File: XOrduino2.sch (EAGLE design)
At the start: 82 parts, among them J1 2.5mm, J2 2.5mm, J3 2.5mm, J4 2.5mm, J5 Batt In, J6 MOT R, J7 MOT L, P1 10k, Q1 ALS-PT204-6C/L177, SW1 RESET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

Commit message: v7: Update USB mini-B footprint & bom; more heat sink area for motor driver.
Went through and widened power traces as much as I could, as well.
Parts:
- JP9: device xorduino:SOLDERJUMPERBOT-VIA-NOCONFLICT -> xorduino:SOLDERJUMPERBOT-NOCONFLICT
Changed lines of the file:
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@@
 <part name="JP8" library="xorduino" deviceset="SOLDERJUMPER" device="BOT-VIA-NOCONFLICT" value="N/C"/>
 <part name="JP7" library="xorduino" deviceset="SOLDERJUMPER" device="BOT-VIA-NOCONFLICT" value="N/C"/>
-<part name="JP9" library="xorduino" deviceset="SOLDERJUMPER" device="BOT-VIA-NOCONFLICT" value="N/C"/>
+<part name="JP9" library="xorduino" deviceset="SOLDERJUMPER" device="BOT-NOCONFLICT" value="N/C"/>
 <part name="JP1" library="xorduino" deviceset="SOLDERJUMPER" device="NOCONFLICT" value="N/C"/>
 <part name="JP10" library="xorduino" deviceset="SOLDERJUMPER" device="BOT-VIA-NOCONFLICT" value="N/C"/>
@@
 <text x="-120.142" y="-31.496" size="1.27" layer="97">optional</text>
 <text x="169.926" y="43.434" size="1.27" layer="97">optional</text>
-<text x="189.23" y="-58.928" size="2.54" layer="97">6</text>
+<text x="189.23" y="-58.928" size="2.54" layer="97">7</text>
 <text x="192.024" y="-69.088" size="2.54" layer="97">CSA</text>
 <text x="40.64" y="30.48" size="3.81" layer="94" ratio="10" rot="MR0">Scratch Sensor Board</text>

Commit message: Minor silkscreen tweaks, extend L3 pads a hair.
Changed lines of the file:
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@@
 <text x="-120.142" y="-31.496" size="1.27" layer="97">optional</text>
 <text x="169.926" y="43.434" size="1.27" layer="97">optional</text>
-<text x="189.23" y="-58.928" size="2.54" layer="97">7</text>
+<text x="189.23" y="-58.928" size="2.54" layer="97">8</text>
 <text x="192.024" y="-69.088" size="2.54" layer="97">CSA</text>
 <text x="40.64" y="30.48" size="3.81" layer="94" ratio="10" rot="MR0">Scratch Sensor Board</text>

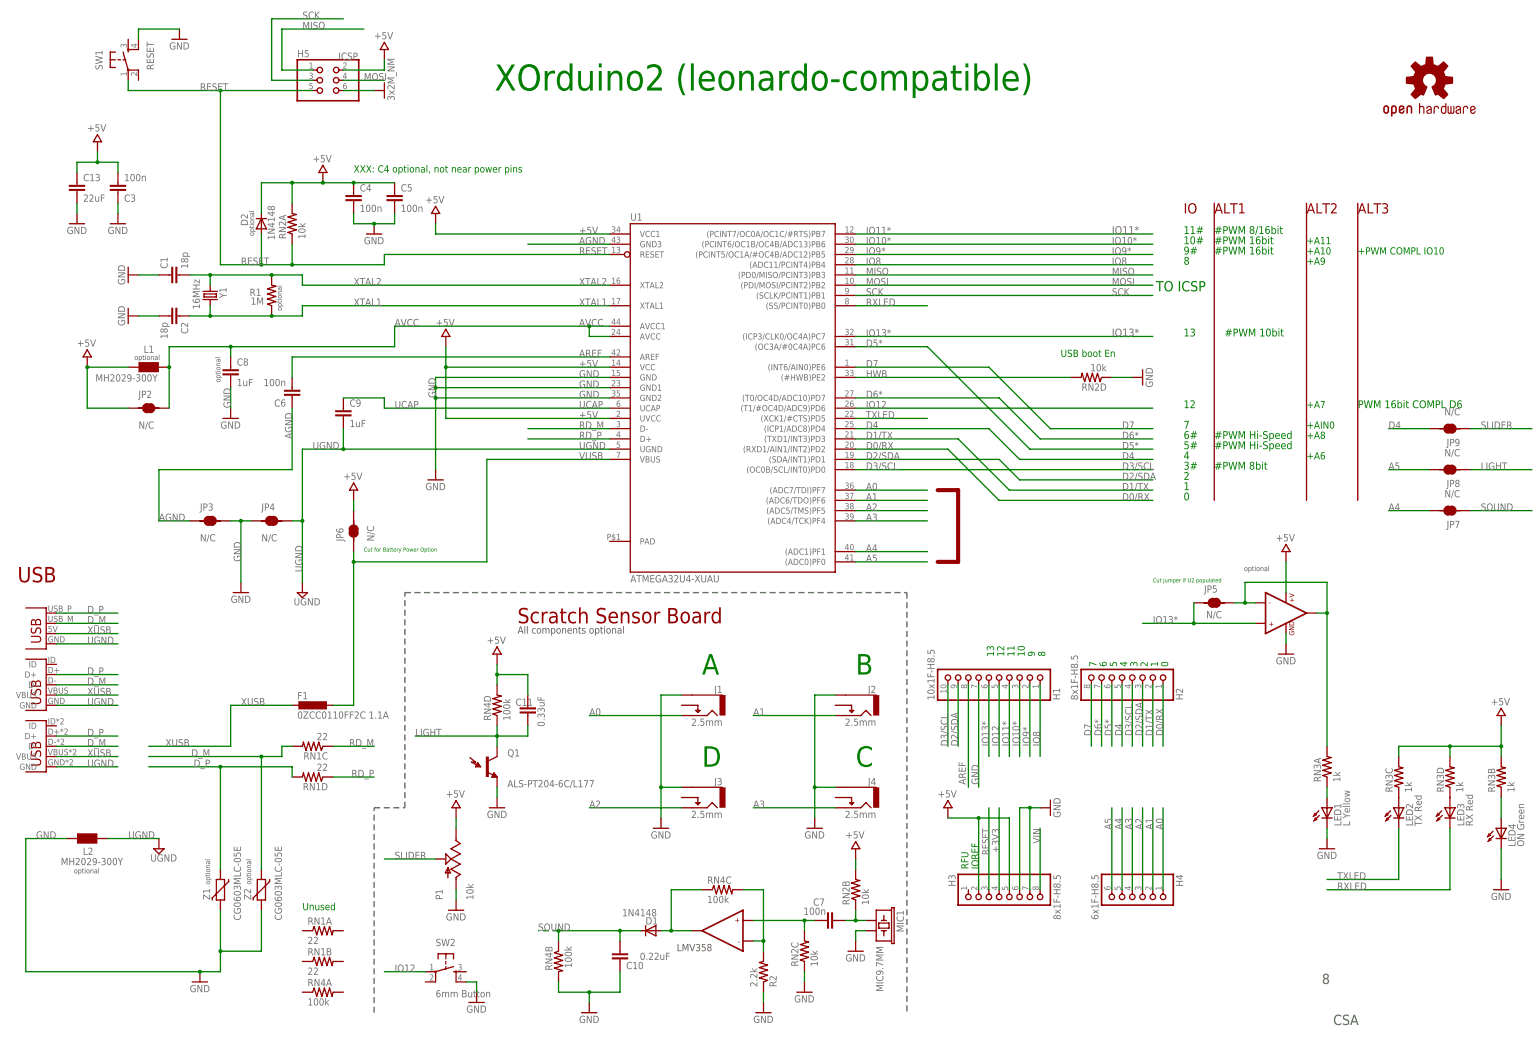
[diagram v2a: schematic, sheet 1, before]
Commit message: XOrduino2 v8.  Rename nets for better manual auditing, silkscreen tweaks.
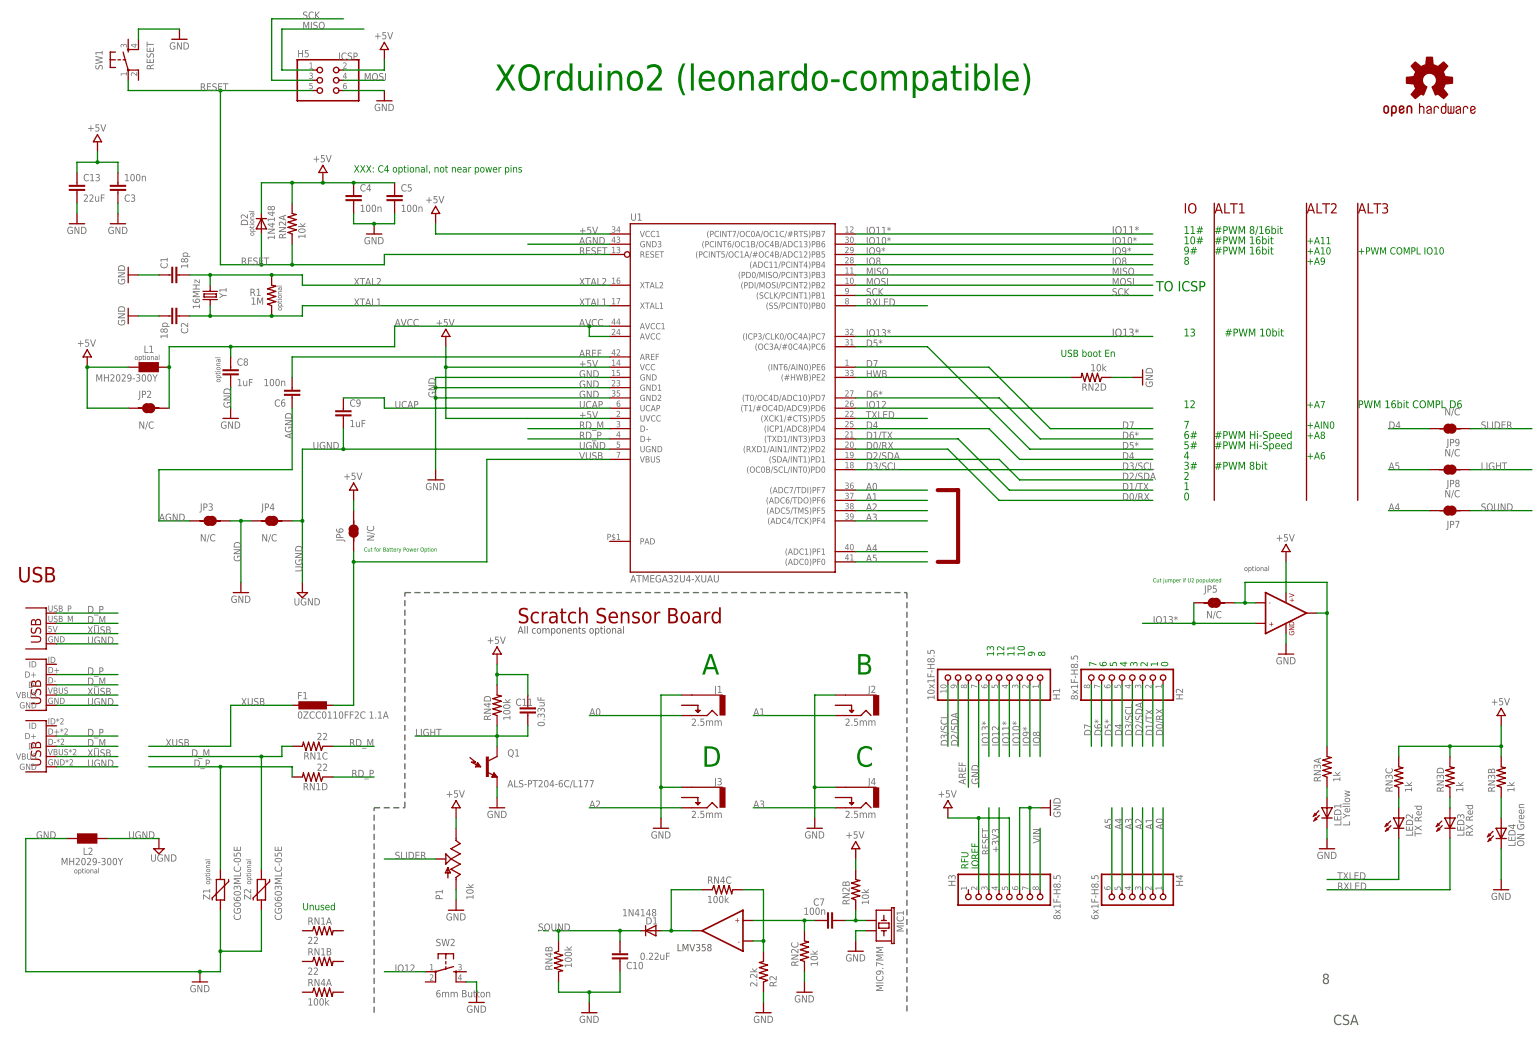
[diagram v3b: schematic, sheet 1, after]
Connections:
- net N$1 renamed LED3_ANODE
- net N$10 renamed U4_VINT
- net N$11 renamed OPAMP1_P
- net N$12 renamed U4_NFAULT
- net N$13 renamed U6_ANODE
- net N$14 renamed U3_CONT
- net N$15 renamed U5_ANODE
- net N$16 renamed OPAMP1_OUT
- net N$18 renamed LED5_CATHODE
- net N$19 renamed U4_BISEN
- net N$2 renamed LED1_ANODE
- net N$20 renamed U4_AISEN
- net N$21 renamed U5_COLLECTOR
- net N$22 renamed U6_COLLECTOR
- net N$3 renamed LED4_ANODE
- net N$4 renamed LED2_ANODE
- net N$5 renamed OPAMP1_M
- net N$6 renamed IO13_MIRROR
- net N$7 renamed U4_VCP
- net N$8 renamed U4_NSLEEP
- net N$9 renamed MIC_IN
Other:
- moved on the sheet: LED2, LED3
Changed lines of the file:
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@@
 <parts>
 <part name="H5" library="SmartPrj" deviceset="PINHD-2X3" device="" value="ICSP"/>
-<part name="GND1" library="supply1" deviceset="GND" device="" value="3x2M_NM"/>
+<part name="GND1" library="supply1" deviceset="GND" device="" value="GND"/>
 <part name="H2" library="SmartPrj" deviceset="PINHD-1X8" device="" value="8x1F-H8.5"/>
 <part name="H4" library="SmartPrj" deviceset="PINHD-1X6" device="" value="6x1F-H8.5"/>
@@
 <attribute name="VALUE" x="-54.61" y="170.18" size="1.778" layer="96"/>
 </instance>
-<instance part="GND1" gate="1" x="-43.18" y="162.56" rot="R90"/>
+<instance part="GND1" gate="1" x="-43.18" y="160.02"/>
 <instance part="H2" gate="A" x="139.7" y="17.78" rot="MR90"/>
 <instance part="H4" gate="A" x="142.24" y="-38.1" rot="R270"/>
@@
 <instance part="GND20" gate="1" x="-81.28" y="81.28"/>
 <instance part="GND23" gate="1" x="144.78" y="91.44" rot="R90"/>
-<instance part="LED2" gate="G$1" x="208.28" y="-15.24"/>
-<instance part="LED3" gate="G$1" x="220.98" y="-15.24"/>
+<instance part="LED2" gate="G$1" x="208.28" y="-17.78"/>
+<instance part="LED3" gate="G$1" x="220.98" y="-17.78"/>
 <instance part="H3" gate="A" x="111.76" y="-38.1" rot="MR270"/>
 <instance part="H1" gate="A" x="109.22" y="17.78" rot="MR90"/>
@@
 <net name="GND" class="2">
 <segment>
-<wire x1="-45.72" y1="162.56" x2="-53.34" y2="162.56" width="0.1524" layer="91"/>
+<wire x1="-43.18" y1="162.56" x2="-53.34" y2="162.56" width="0.1524" layer="91"/>
 <pinref part="GND1" gate="1" pin="GND"/>
 <pinref part="H5" gate="A" pin="6"/>
@@
 </segment>
 </net>
-<net name="N$3" class="0">
+<net name="LED4_ANODE" class="0">
 <segment>
 <wire x1="233.68" y1="-17.78" x2="233.68" y2="-12.7" width="0.1524" layer="91"/>
@@
 </segment>
 </net>
-<net name="N$2" class="0">
+<net name="LED1_ANODE" class="0">
 <segment>
 <wire x1="190.5" y1="-10.16" x2="190.5" y2="-12.7" width="0.1524" layer="91"/>
@@
 <segment>
 <wire x1="190.5" y1="-35.56" x2="220.98" y2="-35.56" width="0.1524" layer="91"/>
-<wire x1="220.98" y1="-35.56" x2="220.98" y2="-20.32" width="0.1524" layer="91"/>
+<wire x1="220.98" y1="-35.56" x2="220.98" y2="-22.86" width="0.1524" layer="91"/>
 <label x="193.04" y="-35.56" size="1.778" layer="95"/>
 <pinref part="LED3" gate="G$1" pin="C"/>
@@
 <net name="TXLED" class="0">
 <segment>
-<wire x1="208.28" y1="-20.32" x2="208.28" y2="-33.02" width="0.1524" layer="91"/>
+<wire x1="208.28" y1="-22.86" x2="208.28" y2="-33.02" width="0.1524" layer="91"/>
 <wire x1="208.28" y1="-33.02" x2="190.5" y2="-33.02" width="0.1524" layer="91"/>
 <label x="193.04" y="-33.02" size="1.778" layer="95"/>
@@
 </segment>
 </net>
-<net name="N$9" class="0">
+<net name="MIC_IN" class="0">
 <segment>
 <wire x1="76.2" y1="-43.18" x2="73.66" y2="-43.18" width="0.1524" layer="91"/>
@@
 </segment>
 </net>
-<net name="N$11" class="0">
+<net name="OPAMP1_P" class="0">
 <segment>
 <wire x1="63.5" y1="-43.18" x2="60.96" y2="-43.18" width="0.1524" layer="91"/>
@@
 </segment>
 </net>
-<net name="N$5" class="0">
+<net name="OPAMP1_M" class="0">
 <segment>
 <wire x1="48.26" y1="-48.26" x2="50.8" y2="-48.26" width="0.1524" layer="91"/>
@@
 </segment>
 </net>
-<net name="N$16" class="0">
+<net name="OPAMP1_OUT" class="0">
 <segment>
 <wire x1="35.56" y1="-35.56" x2="27.94" y2="-35.56" width="0.1524" layer="91"/>
@@
 </segment>
 </net>
-<net name="N$6" class="0">
+<net name="IO13_MIRROR" class="0">
 <segment>
 <pinref part="U2" gate="G$1" pin="OUT1"/>
@@
 </segment>
 </net>
-<net name="N$1" class="0">
+<net name="LED3_ANODE" class="0">
 <segment>
 <pinref part="LED3" gate="G$1" pin="A"/>
 <pinref part="RN3" gate="D" pin="1"/>
-</segment>
-</net>
-<net name="N$4" class="0">
+<wire x1="220.98" y1="-15.24" x2="220.98" y2="-12.7" width="0.1524" layer="91"/>
+</segment>
+</net>
+<net name="LED2_ANODE" class="0">
 <segment>
 <pinref part="LED2" gate="G$1" pin="A"/>
 <pinref part="RN3" gate="C" pin="1"/>
+<wire x1="208.28" y1="-15.24" x2="208.28" y2="-12.7" width="0.1524" layer="91"/>
 </segment>
 </net>
@@
 </busses>
 <nets>
-<net name="N$7" class="0">
+<net name="U4_VCP" class="0">
 <segment>
 <pinref part="C15" gate="G$1" pin="1"/>
@@
 </segment>
 </net>
-<net name="N$10" class="0">
+<net name="U4_VINT" class="0">
 <segment>
 <pinref part="U4" gate="G$1" pin="VINT"/>
@@
 </segment>
 </net>
-<net name="N$8" class="0">
+<net name="U4_NSLEEP" class="0">
 <segment>
 <pinref part="U4" gate="G$1" pin="NSLEEP"/>
@@
 </segment>
 </net>
-<net name="N$12" class="0">
+<net name="U4_NFAULT" class="0">
 <segment>
 <pinref part="U4" gate="G$1" pin="NFAULT"/>
@@
 </segment>
 </net>
-<net name="N$15" class="0">
+<net name="U5_ANODE" class="0">
 <segment>
 <pinref part="U5" gate="G$1" pin="A"/>
@@
 </segment>
 </net>
-<net name="N$13" class="0">
+<net name="U6_ANODE" class="0">
 <segment>
 <pinref part="U6" gate="G$1" pin="A"/>
@@
 </segment>
 </net>
-<net name="N$14" class="0">
+<net name="U3_CONT" class="0">
 <segment>
 <pinref part="U3" gate="G$1" pin="CONT"/>
@@
 </segment>
 </net>
-<net name="N$19" class="0">
+<net name="U4_BISEN" class="0">
 <segment>
 <pinref part="U4" gate="G$1" pin="BISEN"/>
@@
 </segment>
 </net>
-<net name="N$20" class="0">
+<net name="U4_AISEN" class="0">
 <segment>
 <pinref part="RN7" gate="C" pin="1"/>
@@
 </segment>
 </net>
-<net name="N$18" class="0">
+<net name="LED5_CATHODE" class="0">
 <segment>
 <pinref part="LED5" gate="G$1" pin="C"/>
@@
 </segment>
 </net>
-<net name="N$21" class="0">
+<net name="U5_COLLECTOR" class="0">
 <segment>
 <pinref part="RN5" gate="C" pin="2"/>
@@
 </segment>
 </net>
-<net name="N$22" class="0">
+<net name="U6_COLLECTOR" class="0">
 <segment>
 <pinref part="RN5" gate="D" pin="2"/>
